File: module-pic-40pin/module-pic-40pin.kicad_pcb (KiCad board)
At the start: 2 copper layers, 93 x 61.9 mm, 27 parts, among them J1 input_power, J2 ANALOG, J3 icsp, J4 PORTB, J5 PORTC, J6 Conn_02x04_Odd_Even, J7 RB0_CONN, J8 PORTD, SW1 reset, SW2 EXT_INT0, U1 PIC16F877A-IP, Y1 20MHz

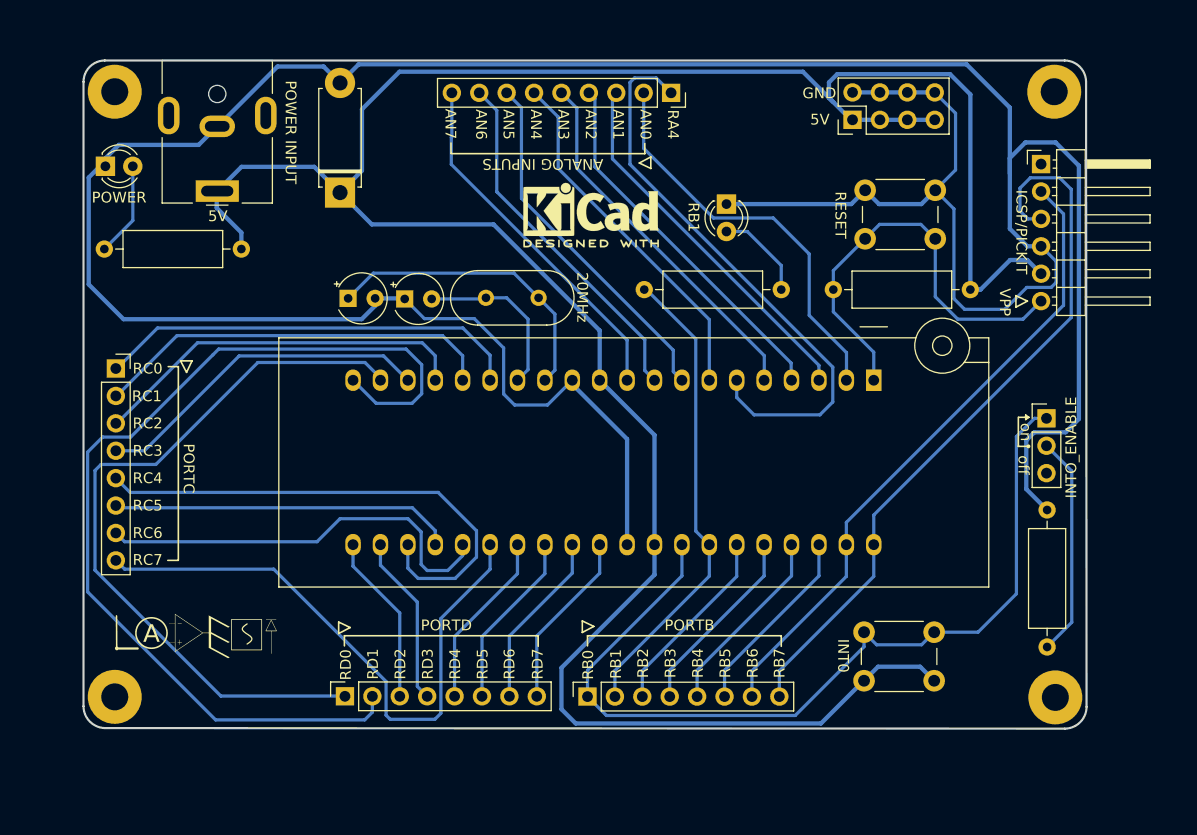
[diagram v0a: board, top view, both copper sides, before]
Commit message: changing module-pic-40pin layout
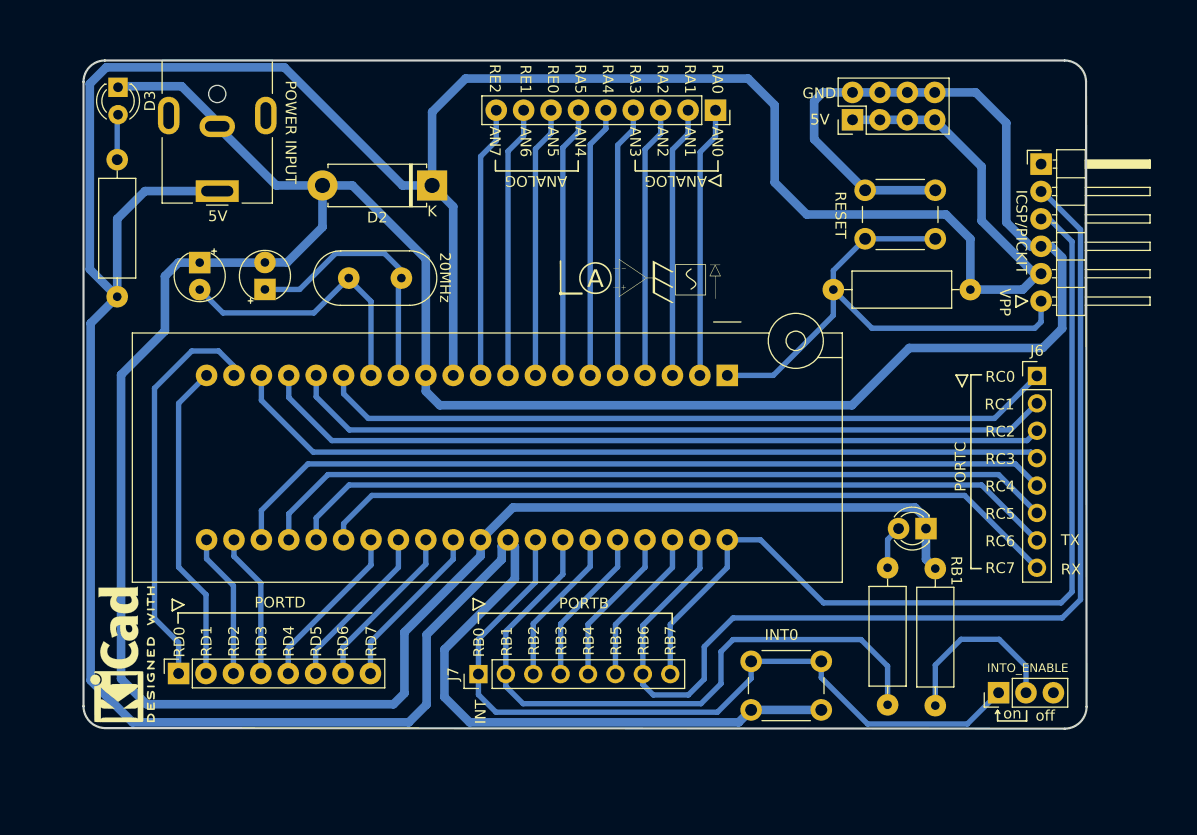
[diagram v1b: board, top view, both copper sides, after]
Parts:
- removed the REF** at (62.1, 32.3)
- removed the REF** at (149.3, 88.4)
- removed the REF** at (149.1, 32.3)
- removed the REF** at (62.1, 88.3)
- D2: renamed from D3; value D_Zener -> ZENER
- D3: renamed from D2; value LED_POWER -> LED_PWR
- J1: renamed from J7; value RB0_CONN -> rb0_enable
- J2: renamed from J1; value input_power -> power_input
- J3: renamed from J6; value Conn_02x04_Odd_Even -> power
- J6: renamed from J5; footprint Connector_PinSocket_2.54mm:PinSocket_1x08_P2.54mm_Vertical -> Connector_PinHeader_2.54mm:PinHeader_1x08_P2.54mm_Vertical
- J7: renamed from J4; footprint Connector_PinSocket_2.54mm:PinSocket_1x08_P2.54mm_Vertical -> Connector_PinHeader_2.54mm:PinHeader_1x08_P2.54mm_Vertical
- R2: renamed from R4; value 330 -> 10k
- R4: renamed from R1; value 10k -> 330
- SW2: renamed from SW1; value reset -> RESET
- moved J6 85.4 mm to (147.5, 58.6)
- moved REF** 59.5 mm to (62.8, 84.4), turned to 90 degrees
- moved G*** 52.7 mm to (110.7, 49.8)
- moved D1 35.3 mm to (137.3, 72.7), turned to 180 degrees
- moved R2 27.6 mm to (133.7, 76.4), turned to -90 degrees
- moved J1 25.8 mm to (144.0, 88.0), turned to 90 degrees
- moved C2 19.3 mm to (70.0, 48.1), turned to -90 degrees
- moved J8 15.6 mm to (68.0, 86.2)
- moved U1 13.6 mm to (118.8, 58.5)
- moved Y1 12.8 mm to (83.8, 49.5)
- moved R1 11.7 mm to (138.1, 89.2)
- moved SW1 10.8 mm to (121.1, 85.0)
- moved J7 10.3 mm to (95.8, 86.2)
- moved D2 8.56 mm to (91.5, 40.9), turned to 180 degrees
- moved R3 8.37 mm to (62.3, 38.6), turned to -90 degrees
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- renumbered J3 to J4, J2 to J5, R2 to R1, SW2 to SW1
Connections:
- net /AN4 renamed /RA5
- net /AN5 renamed /RE0
- net /AN6 renamed /RE1
- net /AN7 renamed /RE2
- J5 pad 1: /RA4 -> /RA0
- J5 pad 2: /AN0 -> /RA1
- J5 pad 3: /AN1 -> /RA2
- J5 pad 4: /AN2 -> /RA3
- J5 pad 5: /AN3 -> /RA4
- U1 pad 2: /AN0 -> /RA0
- U1 pad 3: /AN1 -> /RA1
- U1 pad 4: /AN2 -> /RA2
- U1 pad 5: /AN3 -> /RA3
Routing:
- net +5V: track 235.0 -> 342.6 mm
- net /RD1: track 91.9 -> 29.8 mm
- net /RC3: track 31.6 -> 76.4 mm
- net /RC5: track 31.9 -> 74.7 mm
- net /RB6: track 59.6 -> 101.4 mm
- net /RC2: track 35.5 -> 73.4 mm
- net /AN0: track 37.7 -> 0.00 mm
- net /AN1: track 34.7 -> 0.00 mm
- net /AN3: track 34.4 -> 0.00 mm
- net /AN2: track 34.4 -> 0.00 mm
- net /RC1: track 37.5 -> 71.1 mm
- net /RC6: track 38.7 -> 72.2 mm
- net /RD0: track 68.6 -> 37.6 mm
- net /RC4: track 47.6 -> 77.2 mm
- net /RC0: track 39.6 -> 68.5 mm
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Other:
- board text added: "ANALOG"
- board text added: "INT"
- board text added: "RA0"
- board text added: "RA1"
- board text added: "RA2"
- board text added: "RA3"
- board text added: "RA5"
- board text added: "RE0"
- board text added: "RE1"
- board text added: "RE2"
- board text added: "RX"
- board text added: "TX"
- board text removed: "ANALOG INPUTS"
- board text removed: "POWER"

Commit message: update tracks in module-pic-40pin
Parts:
- moved R4 4.95 mm to (123.7, 50.1)
- moved SW2 4.95 mm to (126.7, 40.9)
- moved R2 4.17 mm to (133.9, 80.5)
- moved D1 4.17 mm to (137.5, 76.9)
- moved R1 4.17 mm to (138.4, 93.3)
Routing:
- net GND: track 320.2 -> 352.7 mm
- net +5V: track 342.6 -> 356.6 mm
- net /RB0: track 72.8 -> 86.1 mm
- net /RB6: track 101.4 -> 111.9 mm
- net /VPP: track 49.9 -> 45.7 mm
- net /RB1: track 60.6 -> 64.1 mm
- net /RC7: track 69.6 -> 68.0 mm
- net Net-(C2-Pad2): track 25.9 -> 27.2 mm
- net /RC6: track 72.2 -> 71.2 mm
- net /RC5: track 74.7 -> 73.7 mm
- net Net-(J1-Pad2): track 16.7 -> 17.5 mm
- net /RC0: track 68.5 -> 67.9 mm
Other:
- board size 93 x 61.9 mm -> 106.6 x 73.3 mm

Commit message: update tracks in module-pic-40pin
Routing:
- net GND: track 352.7 -> 370.7 mm
- net +5V: track 356.6 -> 366.9 mm
- net /RB0: track 86.1 -> 95.2 mm
- net /RB1: track 64.1 -> 72.5 mm
- net /RB6: track 111.9 -> 117.9 mm
- net /RB7: track 86.0 -> 89.4 mm
- net /RD4: track 15.6 -> 17.6 mm
- net /RD5: track 15.6 -> 16.8 mm
- net /RD0: track 37.6 -> 38.5 mm
- net Net-(J1-Pad2): track 17.5 -> 16.9 mm
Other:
- board size 106.6 x 73.3 mm -> 104.7 x 73.3 mm

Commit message: update module-pic-40pin project
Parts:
- moved J1 2.53 mm to (143.3, 90.4)
- moved R1 2.53 mm to (137.7, 95.8)
- moved G*** 2.53 mm to (110.1, 52.3)
- moved J5 2.53 mm to (117.1, 36.4)
- moved REF** 2.53 mm to (62.1, 86.8)
- moved C1 2.53 mm to (75.3, 53.0)
- moved D1 2.53 mm to (136.8, 79.4)
- moved J3 2.53 mm to (129.8, 37.3)
- moved J4 2.53 mm to (147.3, 41.4)
- moved J6 2.53 mm to (146.9, 61.0)
- moved J8 2.53 mm to (67.3, 88.6)
- moved SW2 2.53 mm to (126.0, 43.4)
- moved U1 2.53 mm to (118.2, 61.0)
- moved D3 2.53 mm to (61.7, 34.3)
- moved J2 2.53 mm to (70.9, 43.9)
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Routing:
- net +5V: track 366.9 -> 360.7 mm
- net /RB0: track 95.2 -> 89.2 mm
- net GND: track 370.7 -> 368.6 mm
- net /RB6: track 117.9 -> 116.7 mm
- net /RB7: track 89.4 -> 88.8 mm
- net /RB1: track 72.5 -> 72.0 mm
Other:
- board size 104.7 x 73.3 mm -> 102.1 x 68.8 mm

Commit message: update module-pic-40pin
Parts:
- J6, J7: footprint Connector_PinHeader_2.54mm:PinHeader_1x08_P2.54mm_Vertical -> Connector_PinSocket_2.54mm:PinSocket_1x08_P2.54mm_Vertical
- moved J3 46.4 mm to (83.4, 37.6)
- moved R4 11.3 mm to (122.9, 41.3)
- moved D1 11.0 mm to (144.6, 87.1), turned to -90 degrees
- moved D2 9.12 mm to (81.8, 44.4), turned to 0 degrees
- moved SW2 7.13 mm to (132.2, 46.9), turned to -90 degrees
- moved J5 5.14 mm to (118.0, 41.5)
- moved J1 4.71 mm to (142.1, 94.9)
- moved J4 3.94 mm to (144.3, 38.8)
- moved REF** 2.53 mm to (61.4, 89.3)
- moved D3 1.99 mm to (61.6, 36.3)
- moved J2 1.80 mm to (71.0, 45.7)
- moved G*** 1.79 mm to (108.4, 51.8)
- moved R2 1.48 mm to (132.6, 81.7)
- moved R1 1.48 mm to (137.0, 94.4)
- moved C1 1.19 mm to (75.2, 54.2)
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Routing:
- net GND: track 368.6 -> 272.6 mm
- net +5V: track 360.7 -> 287.0 mm
- net /VPP: track 45.7 -> 67.2 mm
- net Net-(D1-Pad2): track 4.05 -> 16.4 mm
- net /RB0: track 89.2 -> 79.1 mm
- net /RB1: track 72.0 -> 66.5 mm
- net /RB6: track 116.7 -> 111.3 mm
- net Net-(J1-Pad2): track 16.9 -> 11.6 mm
- net /RA5: track 25.2 -> 20.5 mm
- net /RE2: track 25.2 -> 20.5 mm
- net /RA2: track 25.2 -> 20.5 mm
- net /RA0: track 25.2 -> 20.5 mm
- net /RA1: track 25.2 -> 20.5 mm
- net /RA3: track 25.2 -> 20.5 mm
- net /RE1: track 25.2 -> 20.7 mm
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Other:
- board size 102.1 x 68.8 mm -> 98.3 x 65 mm
- board text removed: "ANALOG"
